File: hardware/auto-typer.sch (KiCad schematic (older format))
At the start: 29 parts, among them IC1 ATMEGA88A-P, M1 DC_motor, P1 Power_in, Q1 PHP36N03LT, Q2 PHP36N03LT, Q3 PHP36N03LT, Q4 PHP36N03LT, Q5 PHP36N03LT, Q6 PHP36N03LT, SW1 SW_PUSH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

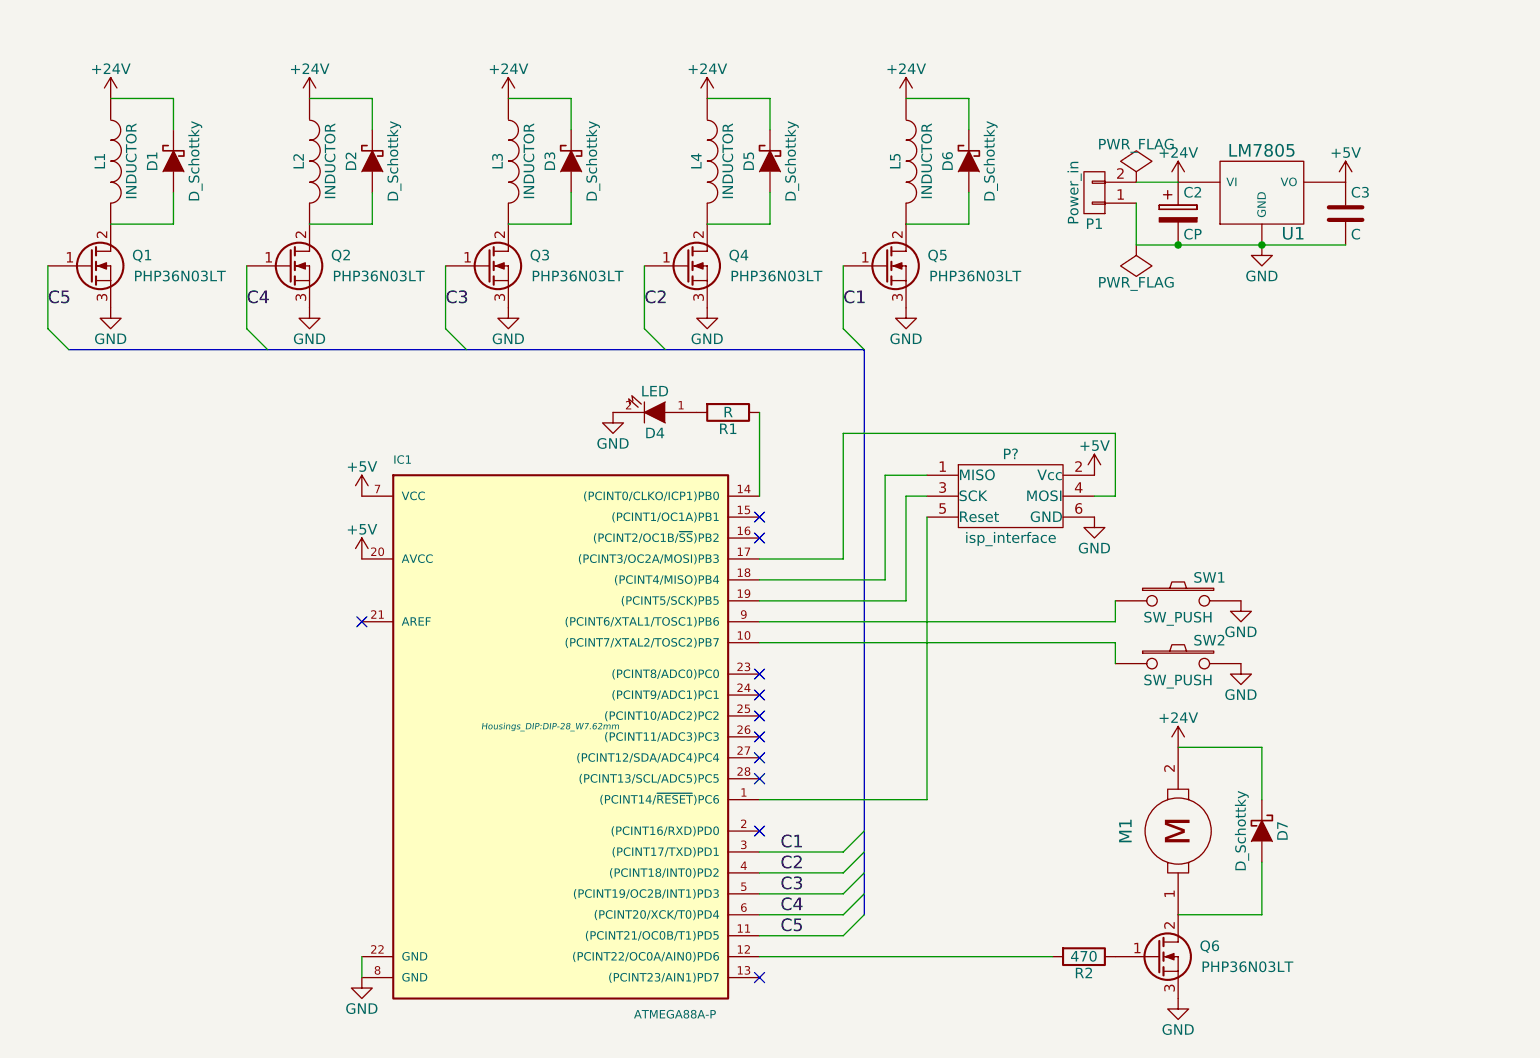
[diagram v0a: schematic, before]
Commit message: Remove startup 65 ms delay that causes coils to pull and cause problems
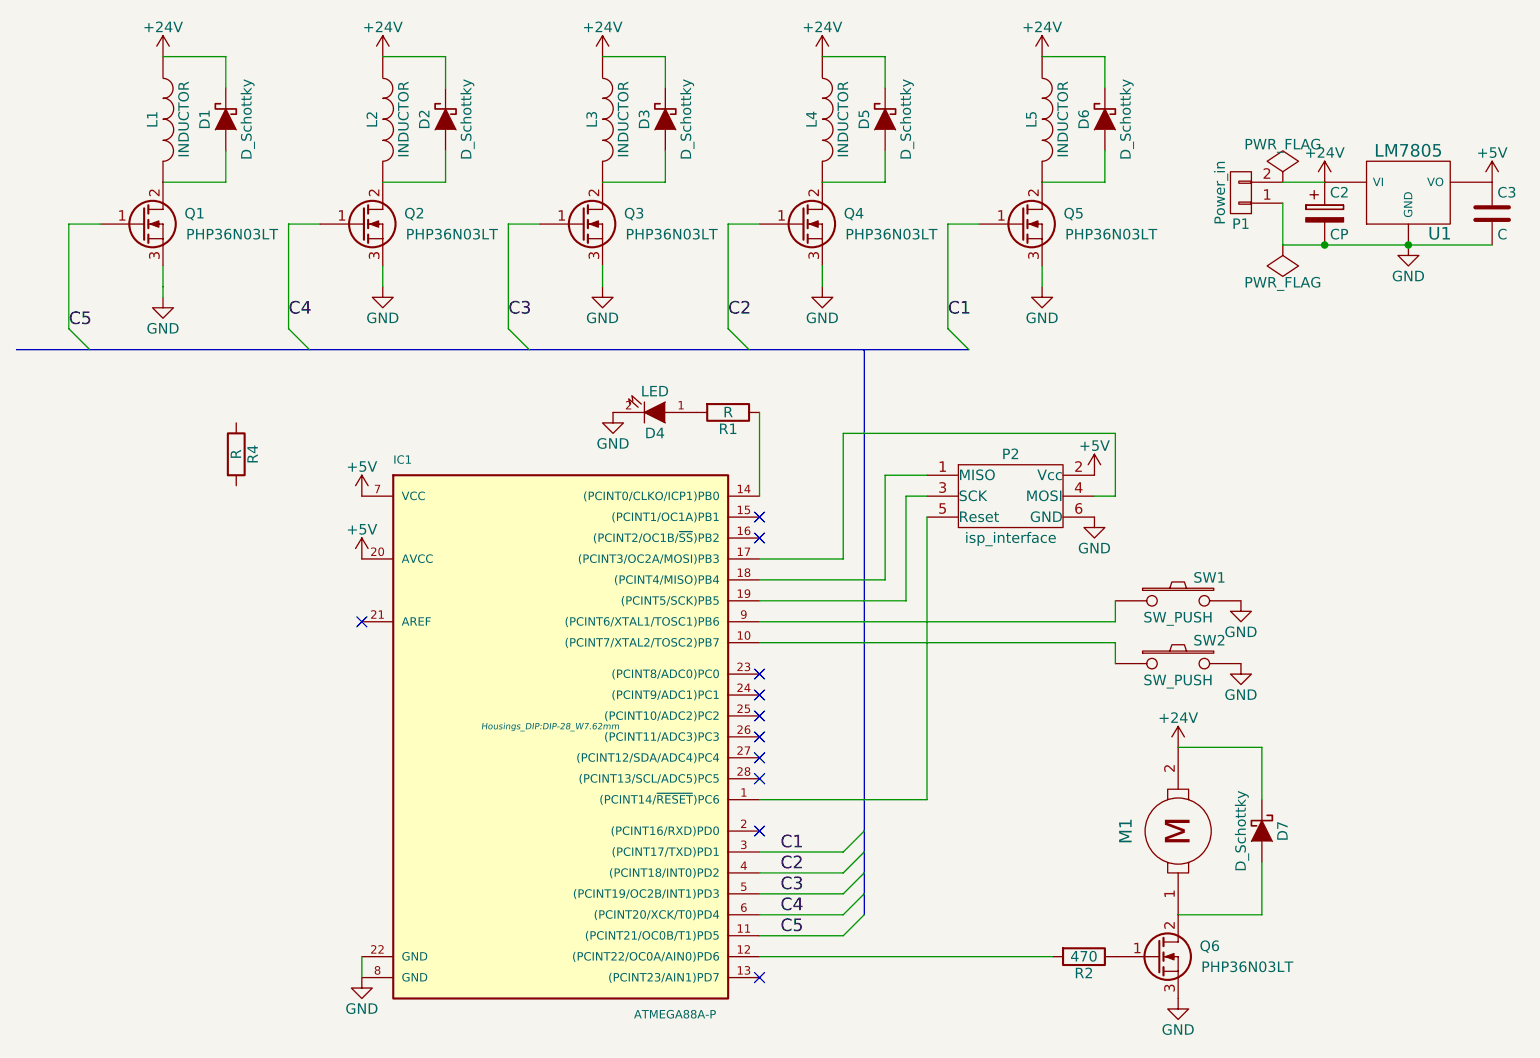
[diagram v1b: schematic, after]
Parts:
- added R4: R, symbol R
- gave numbers to parts that had none: 1
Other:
- moved on the sheet: C2, C3, D1, D2, D3, D5, D6, L1, L2, L3, L4, L5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
